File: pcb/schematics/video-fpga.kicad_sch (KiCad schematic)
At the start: 49 parts

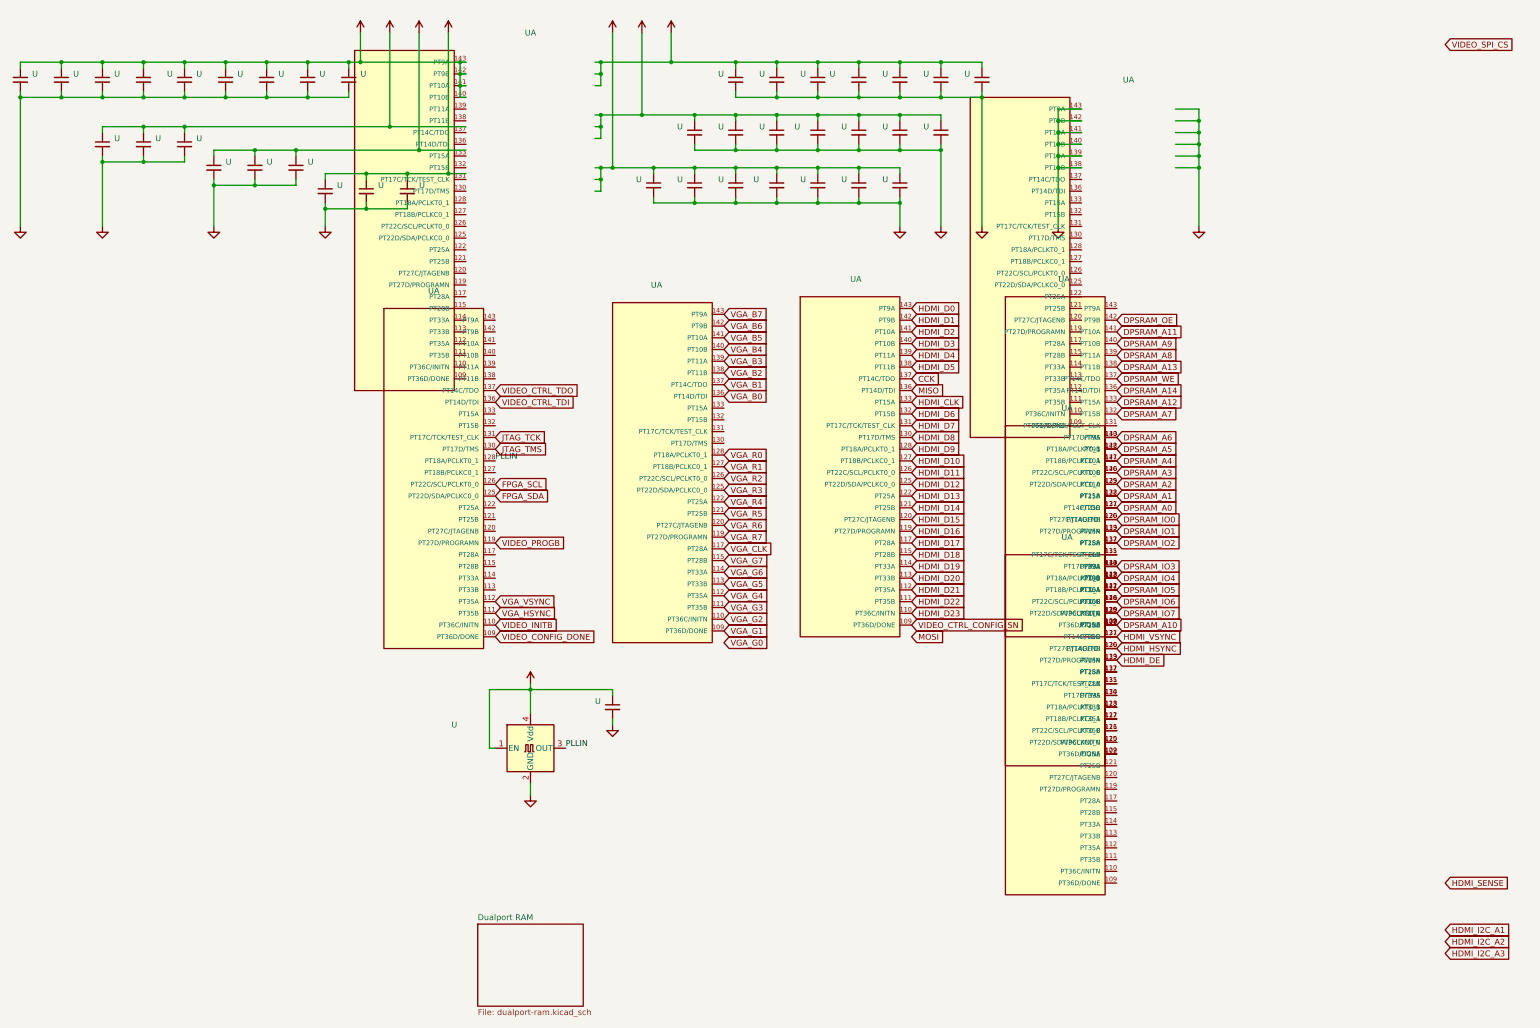
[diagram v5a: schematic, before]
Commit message: add hdmi sense to video controller
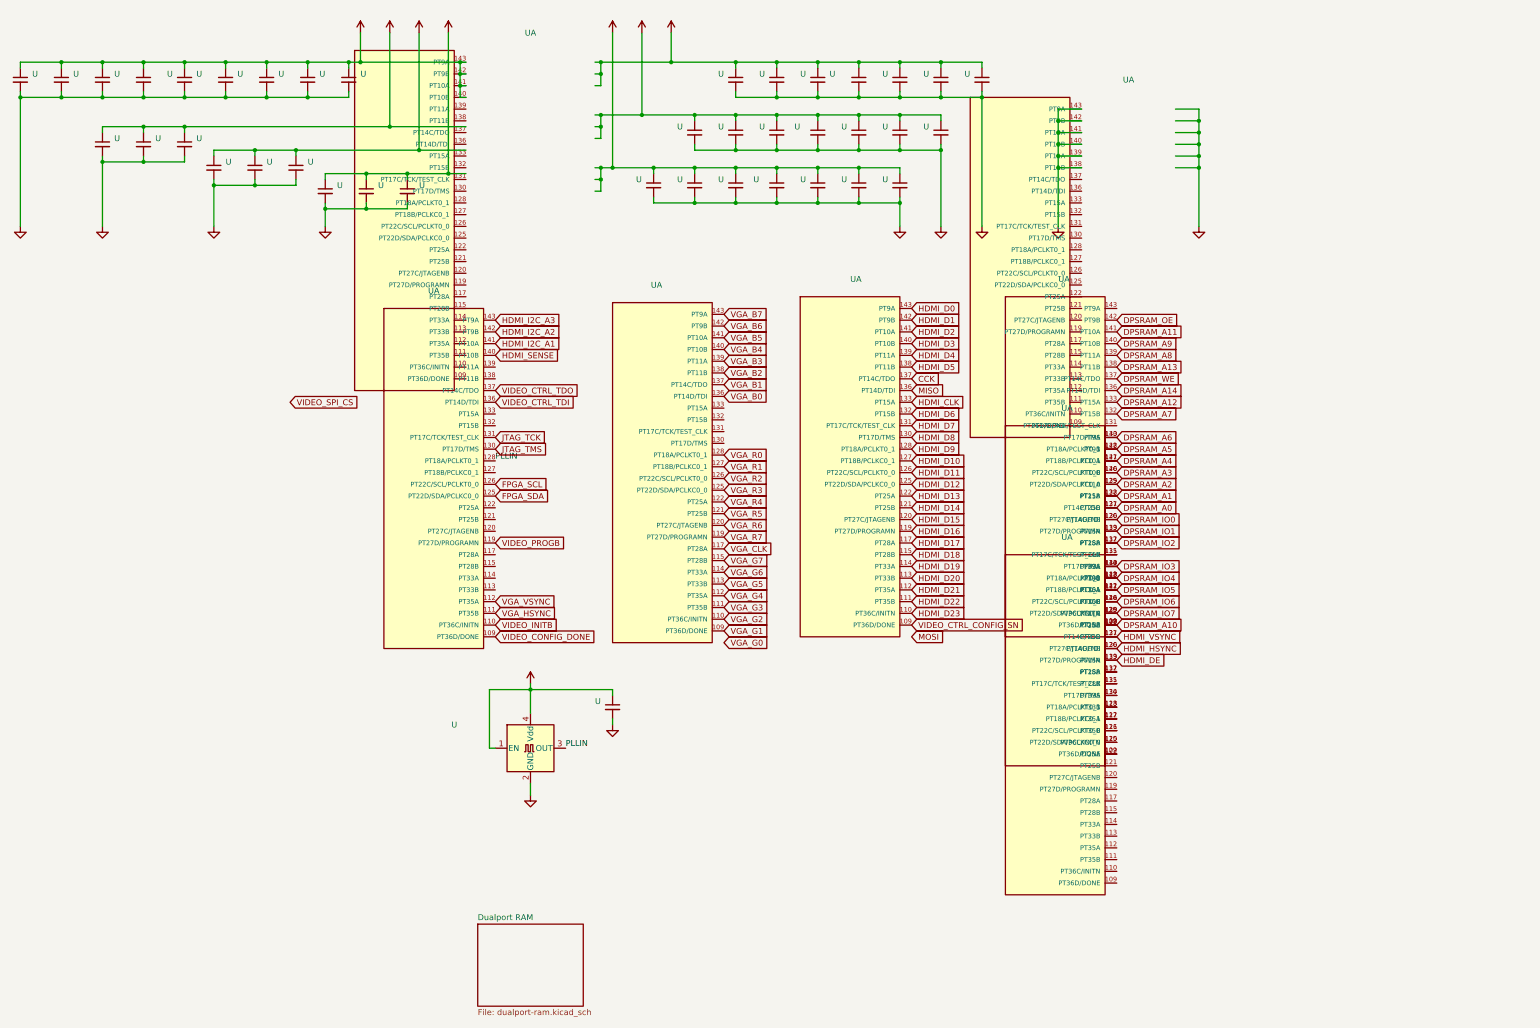
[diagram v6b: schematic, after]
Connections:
- net HDMI_I2C_A1: now also U.141 (PT10A)
- net HDMI_I2C_A2: now also U.142 (PT9B)
- net HDMI_I2C_A3: now also U.143 (PT9A)
- net HDMI_SENSE: now also U.140 (PT10B)
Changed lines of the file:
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@@
     )
   )
-  (global_label "HDMI_SENSE" (shape input) (at 325.12 205.74 0)
-    (effects (font (size 1.27 1.27)) (justify left))
-    (property "Intersheetrefs" "${INTERSHEET_REFS}" (id 0) (at 337.8201 205.74 0)
+  (global_label "HDMI_SENSE" (shape input) (at 119.38 91.44 0)
+    (effects (font (size 1.27 1.27)) (justify left))
+    (property "Intersheetrefs" "${INTERSHEET_REFS}" (id 0) (at 132.0801 91.44 0)
       (effects (font (size 1.27 1.27)) (justify left))
     )
@@
     )
   )
-  (global_label "HDMI_I2C_A1" (shape input) (at 325.12 215.9 0)
-    (effects (font (size 1.27 1.27)) (justify left))
-    (property "Intersheetrefs" "${INTERSHEET_REFS}" (id 0) (at 337.8201 215.9 0)
+  (global_label "HDMI_I2C_A1" (shape input) (at 119.38 88.9 0)
+    (effects (font (size 1.27 1.27)) (justify left))
+    (property "Intersheetrefs" "${INTERSHEET_REFS}" (id 0) (at 132.0801 88.9 0)
       (effects (font (size 1.27 1.27)) (justify left))
     )
@@
     )
   )
-  (global_label "HDMI_I2C_A3" (shape input) (at 325.12 220.98 0)
-    (effects (font (size 1.27 1.27)) (justify left))
-    (property "Intersheetrefs" "${INTERSHEET_REFS}" (id 0) (at 337.8201 220.98 0)
+  (global_label "HDMI_I2C_A3" (shape input) (at 119.38 83.82 0)
+    (effects (font (size 1.27 1.27)) (justify left))
+    (property "Intersheetrefs" "${INTERSHEET_REFS}" (id 0) (at 132.0801 83.82 0)
       (effects (font (size 1.27 1.27)) (justify left))
     )
@@
     )
   )
-  (global_label "HDMI_I2C_A2" (shape input) (at 325.12 218.44 0)
-    (effects (font (size 1.27 1.27)) (justify left))
-    (property "Intersheetrefs" "${INTERSHEET_REFS}" (id 0) (at 337.8201 218.44 0)
+  (global_label "HDMI_I2C_A2" (shape input) (at 119.38 86.36 0)
+    (effects (font (size 1.27 1.27)) (justify left))
+    (property "Intersheetrefs" "${INTERSHEET_REFS}" (id 0) (at 132.0801 86.36 0)
       (effects (font (size 1.27 1.27)) (justify left))
     )
@@
     )
   )
-  (global_label "VIDEO_SPI_CS" (shape input) (at 325.12 24.13 0) (fields_autoplaced)
-    (effects (font (size 1.27 1.27)) (justify left))
-    (property "Intersheetrefs" "${INTERSHEET_REFS}" (id 0) (at 340.904 24.13 0)
-      (effects (font (size 1.27 1.27)) (justify left))
-    )
+  (global_label "VIDEO_SPI_CS" (shape input) (at 74.93 101.6 0) (fields_autoplaced)
+    (effects (font (size 1.27 1.27)) (justify left))
+    (property "Intersheetrefs" "${INTERSHEET_REFS}" (id 0) (at 90.714 101.6 0)
+      (effects (font (size 1.27 1.27)) (justify left))
+    )

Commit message: passed erc and drc
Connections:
- net VIDEO_SPI_CS: now also U.139 (PT11A)
- no-connect marks 0 -> 16
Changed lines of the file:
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@@
   (junction (at 78.74 35.56) (diameter 0) (color 0 0 0 0)
   )
+  (no_connect (at 168.91 102.87))
+  (no_connect (at 168.91 105.41))
+  (no_connect (at 168.91 107.95))
+  (no_connect (at 168.91 110.49))
+  (no_connect (at 254 81.28))
+  (no_connect (at 119.38 96.52))
+  (no_connect (at 119.38 116.84))
+  (no_connect (at 119.38 124.46))
+  (no_connect (at 119.38 104.14))
+  (no_connect (at 119.38 106.68))
+  (no_connect (at 119.38 127))
+  (no_connect (at 119.38 129.54))
+  (no_connect (at 119.38 134.62))
+  (no_connect (at 119.38 137.16))
+  (no_connect (at 119.38 139.7))
+  (no_connect (at 119.38 142.24))
   (wire (pts (xy 215.9 46.99) (xy 215.9 63.5))
     (stroke (width 0) (type default))
@@
     )
   )
-  (global_label "VIDEO_SPI_CS" (shape input) (at 74.93 101.6 0) (fields_autoplaced)
-    (effects (font (size 1.27 1.27)) (justify left))
-    (property "Intersheetrefs" "${INTERSHEET_REFS}" (id 0) (at 90.714 101.6 0)
-      (effects (font (size 1.27 1.27)) (justify left))
-    )
+  (global_label "VIDEO_SPI_CS" (shape input) (at 119.38 93.98 0) (fields_autoplaced)
+    (effects (font (size 1.27 1.27)) (justify left))
+    (property "Intersheetrefs" "${INTERSHEET_REFS}" (id 0) (at 135.164 93.98 0)
+      (effects (font (size 1.27 1.27)) (justify left))
+    )
